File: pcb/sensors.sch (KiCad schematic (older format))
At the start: 7 parts, among them P3 CONN_01X04, P4 CONN_01X04

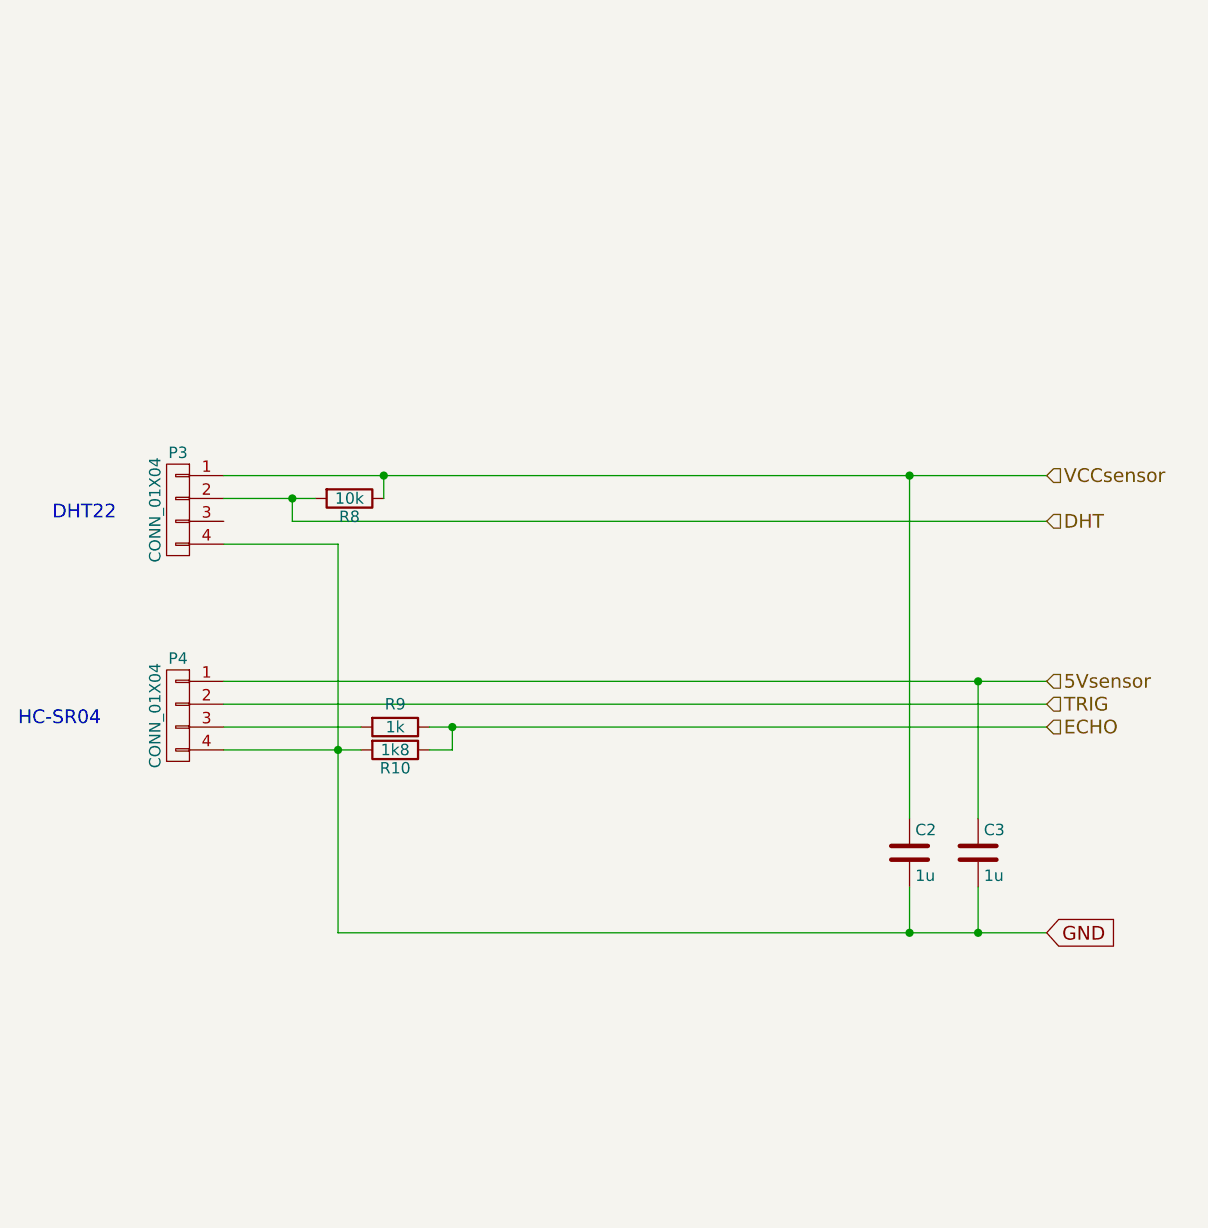
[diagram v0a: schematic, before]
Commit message: added SPI flash and connections for STM32 to control the sensors
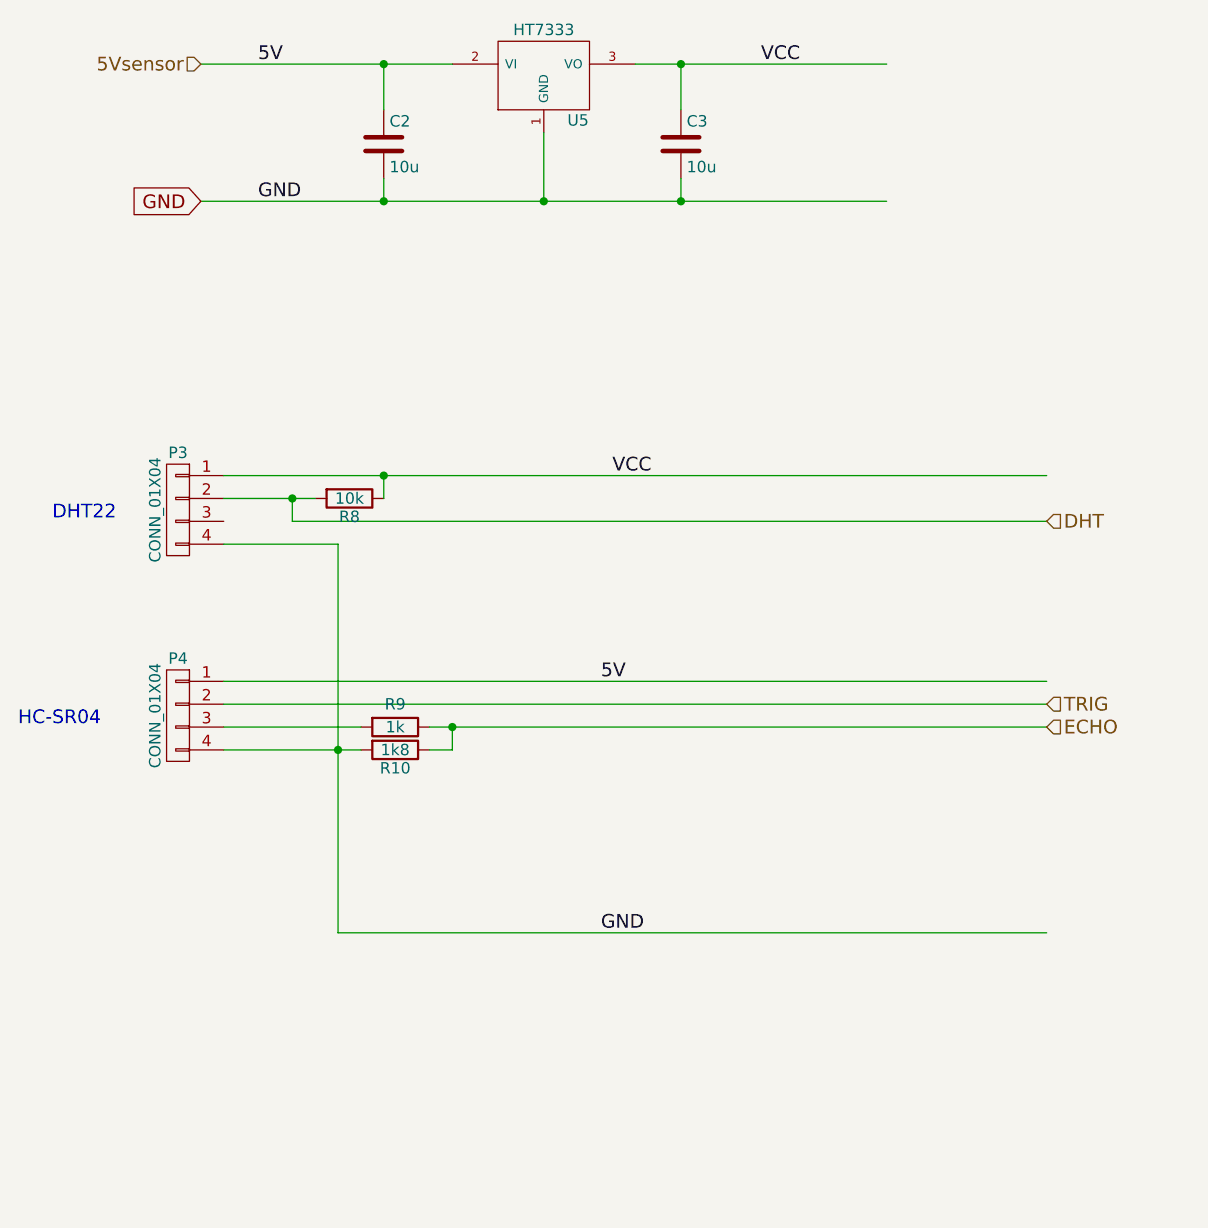
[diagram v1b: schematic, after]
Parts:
- added U5: HT7333, TO_SOT_Packages_SMD:SOT89-3_Housing, symbol HT73xx
- C2, C3: value 1u -> 10u
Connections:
- net labels added: 5V, VCC
- net labels removed: VCCsensor
- wire segments 19 -> 23
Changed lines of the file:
@@
 	4700 3100 8000 3100
 Connection ~ 4700 3000
-Text GLabel 8000 4900 2    60   Input ~ 0
-GND
 Connection ~ 4900 4100
-Text HLabel 8000 3800 2    60   Input ~ 0
+Text HLabel 4300 1100 0    60   Input ~ 0
 5Vsensor
-Text HLabel 8000 2900 2    60   Input ~ 0
-VCCsensor
 Connection ~ 5100 2900
+Wire Wire Line
+	4900 3200 4900 4900
+$Comp
+L HT73xx U5
+U 1 1 57B665D3
+P 5800 1150
+F 0 "U5" H 5950 954 50  0000 C CNN
+F 1 "HT7333" H 5800 1350 50  0000 C CNN
+F 2 "TO_SOT_Packages_SMD:SOT89-3_Housing" H 5800 1150 50  0001 C CNN
+F 3 "" H 5800 1150 50  0000 C CNN
+	1    5800 1150
+	1    0    0    -1
+$EndComp
+$Comp
+L C C2
+U 1 1 57B665DA
+P 5100 1450
+F 0 "C2" H 5125 1550 50  0000 L CNN
+F 1 "10u" H 5125 1350 50  0000 L CNN
+F 2 "Capacitors_SMD:C_0805" H 5138 1300 50  0001 C CNN
+F 3 "" H 5100 1450 50  0000 C CNN
+	1    5100 1450
+	1    0    0    -1
+$EndComp
 $Comp
 L C C3
-U 1 1 57B35820
-P 7700 4550
-F 0 "C3" H 7725 4650 50  0000 L CNN
-F 1 "1u" H 7725 4450 50  0000 L CNN
-F 2 "Capacitors_SMD:C_0805" H 7738 4400 50  0001 C CNN
-F 3 "" H 7700 4550 50  0000 C CNN
-	1    7700 4550
+U 1 1 57B665E1
+P 6400 1450
+F 0 "C3" H 6425 1550 50  0000 L CNN
+F 1 "10u" H 6425 1350 50  0000 L CNN
+F 2 "Capacitors_SMD:C_0805" H 6438 1300 50  0001 C CNN
+F 3 "" H 6400 1450 50  0000 C CNN
+	1    6400 1450
 	1    0    0    -1
 $EndComp
 Wire Wire Line
+	4300 1100 5400 1100
+Wire Wire Line
+	5100 1100 5100 1300
+Connection ~ 5100 1100
+Wire Wire Line
+	5100 1600 5100 1700
+Wire Wire Line
+	4300 1700 7300 1700
+Connection ~ 5800 1700
+Wire Wire Line
+	6400 1700 6400 1600
+Connection ~ 6400 1700
+Wire Wire Line
+	6400 1300 6400 1100
+Connection ~ 6400 1100
+Wire Wire Line
+	5800 1400 5800 1700
+Connection ~ 5100 1700
+Text GLabel 4300 1700 0    60   Input ~ 0
+GND
+Wire Wire Line
+	6200 1100 7300 1100
+Text Label 4550 1700 0    60   ~ 0
+GND
+Text Label 4550 1100 0    60   ~ 0
+5V
+Text Label 6050 3800 0    60   ~ 0
+5V
+Text Label 6100 2900 0    60   ~ 0
+VCC
+Text Label 6750 1100 0    60   ~ 0
+VCC
+Wire Wire Line
 	4900 4900 8000 4900
-Wire Wire Line
-	4900 3200 4900 4900
-$Comp
-L C C2
-U 1 1 57B35A52
-P 7400 4550
-F 0 "C2" H 7425 4650 50  0000 L CNN
-F 1 "1u" H 7425 4450 50  0000 L CNN
-F 2 "Capacitors_SMD:C_0805" H 7438 4400 50  0001 C CNN
-F 3 "" H 7400 4550 50  0000 C CNN
-	1    7400 4550
-	1    0    0    -1
-$EndComp
-Wire Wire Line
-	7700 4900 7700 4700
-Connection ~ 7700 4900
-Wire Wire Line
-	7700 4400 7700 3800
-Connection ~ 7700 3800
-Wire Wire Line
-	7400 4400 7400 2900
-Connection ~ 7400 2900
-Wire Wire Line
-	7400 4700 7400 4900
-Connection ~ 7400 4900
+Text Label 6050 4900 0    60   ~ 0
+GND
 $EndSCHEMATC

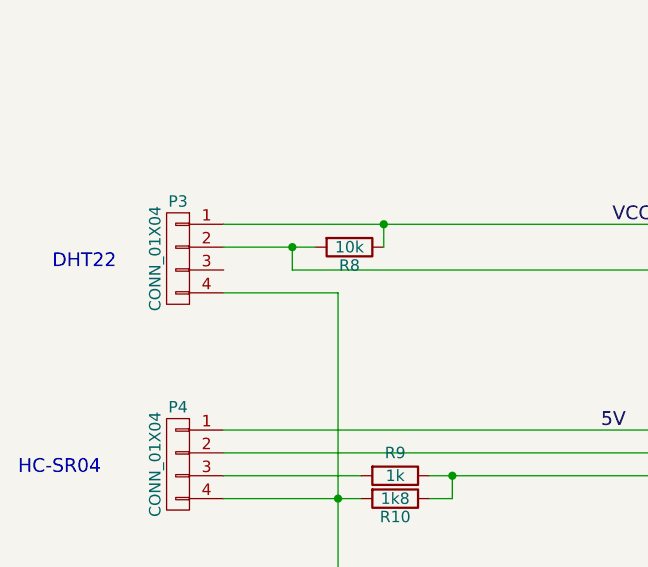
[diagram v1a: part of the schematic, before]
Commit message: PCB simplification
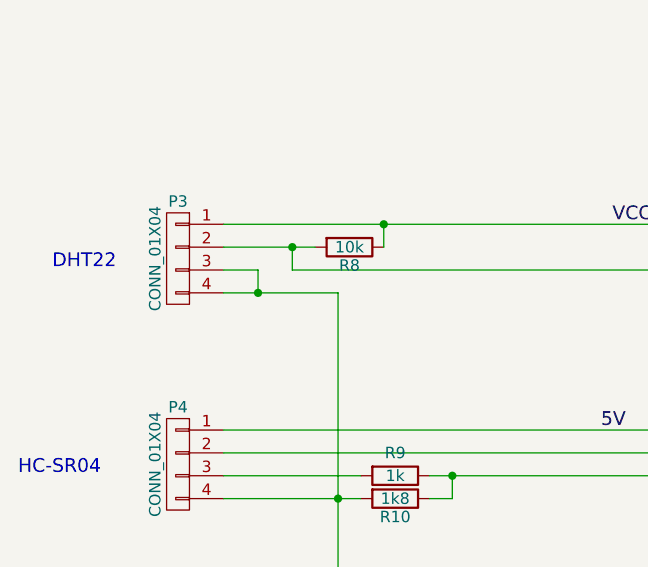
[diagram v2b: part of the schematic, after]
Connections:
- wire segments 23 -> 25
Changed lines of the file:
@@
 Text Label 6050 4900 0    60   ~ 0
 GND
+Wire Wire Line
+	4400 3100 4550 3100
+Wire Wire Line
+	4550 3100 4550 3200
+Connection ~ 4550 3200
 $EndSCHEMATC

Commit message: completed PCB layout first good draft
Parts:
- added P13: CONN_01X02, Pin_Headers:Pin_Header_Straight_1x02, symbol CONN_01X02
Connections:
- net labels added: PiVCC
- wire segments 25 -> 27
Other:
- moved on the sheet: C2, C3, P3, P4, R10, R8, R9, U5
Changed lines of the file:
@@
 L CONN_01X04 P3
 U 1 1 57B344E3
-P 4200 3050
-F 0 "P3" H 4200 3300 50  0000 C CNN
-F 1 "CONN_01X04" V 4300 3050 50  0000 C CNN
-F 2 "Pin_Headers:Pin_Header_Angled_1x04" H 4200 3050 50  0001 C CNN
-F 3 "" H 4200 3050 50  0000 C CNN
-	1    4200 3050
+P 4200 4250
+F 0 "P3" H 4200 4500 50  0000 C CNN
+F 1 "CONN_01X04" V 4300 4250 50  0000 C CNN
+F 2 "Pin_Headers:Pin_Header_Angled_1x04" H 4200 4250 50  0001 C CNN
+F 3 "" H 4200 4250 50  0000 C CNN
+	1    4200 4250
 	-1   0    0    -1
 $EndComp
-Text Notes 3650 3100 0    60   ~ 0
+Text Notes 3650 4300 0    60   ~ 0
 DHT22
 $Comp
 L R R8
 U 1 1 57B344EE
-P 4950 3000
-F 0 "R8" V 5030 3000 50  0000 C CNN
-F 1 "10k" V 4950 3000 50  0000 C CNN
-F 2 "Resistors_SMD:R_0805" V 4880 3000 50  0001 C CNN
-F 3 "" H 4950 3000 50  0000 C CNN
-	1    4950 3000
+P 4950 4200
+F 0 "R8" V 5030 4200 50  0000 C CNN
+F 1 "10k" V 4950 4200 50  0000 C CNN
+F 2 "Resistors_SMD:R_0805" V 4880 4200 50  0001 C CNN
+F 3 "" H 4950 4200 50  0000 C CNN
+	1    4950 4200
 	0    1    1    0
 $EndComp
@@
 L CONN_01X04 P4
 U 1 1 57B344F5
-P 4200 3950
-F 0 "P4" H 4200 4200 50  0000 C CNN
-F 1 "CONN_01X04" V 4300 3950 50  0000 C CNN
-F 2 "Pin_Headers:Pin_Header_Angled_1x04" H 4200 3950 50  0001 C CNN
-F 3 "" H 4200 3950 50  0000 C CNN
-	1    4200 3950
+P 4200 5150
+F 0 "P4" H 4200 5400 50  0000 C CNN
+F 1 "CONN_01X04" V 4300 5150 50  0000 C CNN
+F 2 "Pin_Headers:Pin_Header_Angled_1x04" H 4200 5150 50  0001 C CNN
+F 3 "" H 4200 5150 50  0000 C CNN
+	1    4200 5150
 	-1   0    0    -1
 $EndComp
-Text Notes 3500 4000 0    60   ~ 0
+Text Notes 3500 5200 0    60   ~ 0
 HC-SR04
 $Comp
 L R R9
 U 1 1 57B344FF
-P 5150 4000
-F 0 "R9" V 5050 4000 50  0000 C CNN
-F 1 "1k" V 5150 4000 50  0000 C CNN
-F 2 "Resistors_SMD:R_0805" V 5080 4000 50  0001 C CNN
-F 3 "" H 5150 4000 50  0000 C CNN
-	1    5150 4000
+P 5150 5200
+F 0 "R9" V 5050 5200 50  0000 C CNN
+F 1 "1k" V 5150 5200 50  0000 C CNN
+F 2 "Resistors_SMD:R_0805" V 5080 5200 50  0001 C CNN
+F 3 "" H 5150 5200 50  0000 C CNN
+	1    5150 5200
 	0    1    1    0
 $EndComp
@@
 L R R10
 U 1 1 57B34506
-P 5150 4100
-F 0 "R10" V 5230 4100 50  0000 C CNN
-F 1 "1k8" V 5150 4100 50  0000 C CNN
-F 2 "Resistors_SMD:R_0805" V 5080 4100 50  0001 C CNN
-F 3 "" H 5150 4100 50  0000 C CNN
-	1    5150 4100
+P 5150 5300
+F 0 "R10" V 5230 5300 50  0000 C CNN
+F 1 "1k8" V 5150 5300 50  0000 C CNN
+F 2 "Resistors_SMD:R_0805" V 5080 5300 50  0001 C CNN
+F 3 "" H 5150 5300 50  0000 C CNN
+	1    5150 5300
 	0    1    1    0
 $EndComp
 Wire Wire Line
-	4400 3000 4800 3000
+	4400 4200 4800 4200
 Wire Wire Line
-	5100 2900 5100 3000
+	5100 4100 5100 4200
 Wire Wire Line
-	4400 3800 8000 3800
+	4400 5000 8000 5000
 Wire Wire Line
-	4400 4000 5000 4000
+	4400 5200 5000 5200
 Wire Wire Line
-	5400 4000 5400 4100
-Connection ~ 5400 4000
+	5400 5200 5400 5300
+Connection ~ 5400 5200
 Wire Wire Line
-	4400 2900 8000 2900
+	4400 4100 8000 4100
 Wire Wire Line
-	4400 3200 4900 3200
+	4400 4400 4900 4400
 Wire Wire Line
-	4400 3900 8000 3900
+	4400 5100 8000 5100
 Wire Wire Line
-	5300 4000 8000 4000
+	5300 5200 8000 5200
 Wire Wire Line
-	4400 4100 5000 4100
+	4400 5300 5000 5300
 Wire Wire Line
-	5400 4100 5300 4100
-Text HLabel 8000 3900 2    60   Input ~ 0
+	5400 5300 5300 5300
+Text HLabel 8000 5100 2    60   Input ~ 0
 TRIG
-Text HLabel 8000 4000 2    60   Input ~ 0
+Text HLabel 8000 5200 2    60   Input ~ 0
 ECHO
-Text HLabel 8000 3100 2    60   Input ~ 0
+Text HLabel 8000 4300 2    60   Input ~ 0
 DHT
 Wire Wire Line
-	4700 3000 4700 3100
+	4700 4200 4700 4300
 Wire Wire Line
-	4700 3100 8000 3100
-Connection ~ 4700 3000
-Connection ~ 4900 4100
-Text HLabel 4300 1100 0    60   Input ~ 0
+	4700 4300 8000 4300
+Connection ~ 4700 4200
+Connection ~ 4900 5300
+Text HLabel 4300 2300 0    60   Input ~ 0
 5Vsensor
-Connection ~ 5100 2900
+Connection ~ 5100 4100
 Wire Wire Line
-	4900 3200 4900 4900
+	4900 4400 4900 6100
 $Comp
 L HT73xx U5
 U 1 1 57B665D3
-P 5800 1150
-F 0 "U5" H 5950 954 50  0000 C CNN
-F 1 "HT7333" H 5800 1350 50  0000 C CNN
-F 2 "TO_SOT_Packages_SMD:SOT89-3_Housing" H 5800 1150 50  0001 C CNN
-F 3 "" H 5800 1150 50  0000 C CNN
-	1    5800 1150
+P 5800 2350
+F 0 "U5" H 5950 2154 50  0000 C CNN
+F 1 "HT7333" H 5800 2550 50  0000 C CNN
+F 2 "TO_SOT_Packages_SMD:SOT89-3_Housing" H 5800 2350 50  0001 C CNN
+F 3 "" H 5800 2350 50  0000 C CNN
+	1    5800 2350
 	1    0    0    -1
 $EndComp
@@
 L C C2
 U 1 1 57B665DA
-P 5100 1450
-F 0 "C2" H 5125 1550 50  0000 L CNN
-F 1 "10u" H 5125 1350 50  0000 L CNN
-F 2 "Capacitors_SMD:C_0805" H 5138 1300 50  0001 C CNN
-F 3 "" H 5100 1450 50  0000 C CNN
-	1    5100 1450
+P 5100 2650
+F 0 "C2" H 5125 2750 50  0000 L CNN
+F 1 "10u" H 5125 2550 50  0000 L CNN
+F 2 "Capacitors_SMD:C_0805" H 5138 2500 50  0001 C CNN
+F 3 "" H 5100 2650 50  0000 C CNN
+	1    5100 2650
 	1    0    0    -1
 $EndComp
@@
 L C C3
 U 1 1 57B665E1
-P 6400 1450
-F 0 "C3" H 6425 1550 50  0000 L CNN
-F 1 "10u" H 6425 1350 50  0000 L CNN
-F 2 "Capacitors_SMD:C_0805" H 6438 1300 50  0001 C CNN
-F 3 "" H 6400 1450 50  0000 C CNN
-	1    6400 1450
+P 6400 2650
+F 0 "C3" H 6425 2750 50  0000 L CNN
+F 1 "10u" H 6425 2550 50  0000 L CNN
+F 2 "Capacitors_SMD:C_0805" H 6438 2500 50  0001 C CNN
+F 3 "" H 6400 2650 50  0000 C CNN
+	1    6400 2650
 	1    0    0    -1
 $EndComp
 Wire Wire Line
-	4300 1100 5400 1100
+	4300 2300 5400 2300
 Wire Wire Line
-	5100 1100 5100 1300
-Connection ~ 5100 1100
+	5100 2300 5100 2500
+Connection ~ 5100 2300
 Wire Wire Line
-	5100 1600 5100 1700
+	5100 2800 5100 2900
 Wire Wire Line
-	4300 1700 7300 1700
-Connection ~ 5800 1700
+	4300 2900 7300 2900
+Connection ~ 5800 2900
 Wire Wire Line
-	6400 1700 6400 1600
-Connection ~ 6400 1700
+	6400 2900 6400 2800
+Connection ~ 6400 2900
 Wire Wire Line
-	6400 1300 6400 1100
-Connection ~ 6400 1100
+	6400 2500 6400 2300
+Connection ~ 6400 2300
 Wire Wire Line
-	5800 1400 5800 1700
-Connection ~ 5100 1700
-Text GLabel 4300 1700 0    60   Input ~ 0
+	5800 2600 5800 2900
+Connection ~ 5100 2900
+Text GLabel 4300 2900 0    60   Input ~ 0
 GND
 Wire Wire Line
-	6200 1100 7300 1100
-Text Label 4550 1700 0    60   ~ 0
+	6200 2300 7300 2300
+Text Label 4550 2900 0    60   ~ 0
 GND
-Text Label 4550 1100 0    60   ~ 0
+Text Label 4550 2300 0    60   ~ 0
 5V
-Text Label 6050 3800 0    60   ~ 0
+Text Label 6050 5000 0    60   ~ 0
 5V
-Text Label 6100 2900 0    60   ~ 0
+Text Label 6100 4100 0    60   ~ 0
 VCC
-Text Label 6750 1100 0    60   ~ 0
+Text Label 6750 2300 0    60   ~ 0
 VCC
 Wire Wire Line
-	4900 4900 8000 4900
-Text Label 6050 4900 0    60   ~ 0
+	4900 6100 8000 6100
+Text Label 6050 6100 0    60   ~ 0
 GND
 Wire Wire Line
-	4400 3100 4550 3100
+	4400 4300 4550 4300
 Wire Wire Line
-	4550 3100 4550 3200
-Connection ~ 4550 3200
+	4550 4300 4550 4400
+Connection ~ 4550 4400
+Text HLabel 4300 1900 0    60   Input ~ 0
+PiVCC
+$Comp
+L CONN_01X02 P13
+U 1 1 580A18FA
+P 6450 1700
+F 0 "P13" H 6450 1850 50  0000 C CNN
+F 1 "CONN_01X02" V 6550 1700 50  0000 C CNN
+F 2 "Pin_Headers:Pin_Header_Straight_1x02" H 6450 1700 50  0001 C CNN
+F 3 "" H 6450 1700 50  0000 C CNN
+	1    6450 1700
+	0    -1   -1   0
+$EndComp
+Wire Wire Line
+	6500 1900 6500 2300
+Connection ~ 6500 2300
+Wire Wire Line
+	6400 1900 4300 1900
 $EndSCHEMATC
